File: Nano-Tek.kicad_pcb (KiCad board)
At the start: 4 copper layers, 55 x 42 mm, 47 parts, among them CN1 POWER_IN, CN2 USB, CN3 Floppy 34, J1 Sound, J2 USB_Prog, J3 OLED+SER, J4 Encoder, Q1 MMBT3904, U1 STM32F105RBT6, U2 74LCX07, U3 AP2112K-3.3, X1 8MHz

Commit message: Rev 1.1
OLED and Serial pin header changes.
Additional GND point for connecting 2 pin +5V input instead of using a Berg.
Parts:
- added J5: GND, Nano-Tek:GND_Pin, F.Cu at (88.5, 19.9)
- J3: value OLED+SER -> OLED; footprint Connector_PinHeader_2.54mm:PinHeader_1x06_P2.54mm_Vertical -> Connector_PinSocket_2.54mm:PinSocket_1x04_P2.54mm_Vertical
- J4: value Encoder -> Encoder+SER; footprint Connector_PinHeader_2.54mm:PinHeader_1x05_P2.54mm_Vertical -> Connector_PinHeader_2.54mm:PinHeader_1x07_P2.54mm_Vertical
- moved J4 10.8 mm to (41.6, 20.0)
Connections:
- J3 pad 1: SWCLK -> GND
- J3 pad 2: SWDIO -> +3V3
- J3 pad 3: GND -> SCL
- J3 pad 4: +3V3 -> SDA
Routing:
- net ENC_CLK: track 36.9 -> 45.0 mm
- net SDA: track 24.9 -> 19.1 mm
- net ENC_DT: track 35.5 -> 41.3 mm
- net SCL: track 19.9 -> 24.6 mm
- net ENC_SW: track 18.1 -> 22.1 mm
- net GND: vias 82 -> 83
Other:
- board text added: "+5V"
- board text added: "ENC"
- board text added: "Rev 1.1, August 2026 Schematics derived from OpenFlops design by SukkoPera Thanks to: Vinny, Mesarim, Screemo, Kavanoz, Wrangler, Ordyne"
- board text removed: "Rev 1.0, July 2026 Schematics derived from OpenFlops design by SukkoPera Thanks to: Vinny, Mesarim, Screemo, Kavanoz, Wrangler, Ordyne"

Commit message: Rev 1.1
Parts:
- moved J3 0.05 mm to (66.8, 20.0)
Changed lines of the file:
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@@
 	(footprint "Connector_PinSocket_2.54mm:PinSocket_1x04_P2.54mm_Vertical"
 		(layer "F.Cu")
-		(at 66.8 20.05 90)
+		(at 66.8 20 90)
 		(descr "Through hole straight socket strip, 1x04, 2.54mm pitch, single row (from Kicad 4.0.7), script generated")
 		(tags "Through hole socket strip THT 1x04 2.54mm single row")
 		(property "Reference" "J3"
-			(at 0 -2.77 90)
+			(at 0 -2.95 180)
 			(layer "F.SilkS")
 			(effects
@@
 		(tags "Through hole pin header THT 1x07 2.54mm single row")
 		(property "Reference" "J4"
-			(at 0 -2.38 90)
+			(at 0 17.92 180)
 			(layer "F.SilkS")
 			(effects
@@
 	)
 	(segment
-		(start 64.55 35.1)
-		(end 61.45 32)
-		(width 0.3)
-		(layer "F.Cu")
-		(net "SWCLK")
-	)
-	(segment
-		(start 62.75 43.175)
-		(end 62.75 42.275)
-		(width 0.3)
-		(layer "F.Cu")
-		(net "SWCLK")
-	)
-	(segment
-		(start 64.55 40.475)
-		(end 64.55 35.1)
-		(width 0.3)
-		(layer "F.Cu")
-		(net "SWCLK")
-	)
-	(segment
-		(start 61.45 24.58)
-		(end 56.87 20)
-		(width 0.3)
-		(layer "F.Cu")
-		(net "SWCLK")
-	)
-	(segment
-		(start 61.45 32)
-		(end 61.45 24.58)
-		(width 0.3)
-		(layer "F.Cu")
-		(net "SWCLK")
-	)
-	(segment
-		(start 62.75 42.275)
-		(end 64.55 40.475)
-		(width 0.3)
-		(layer "F.Cu")
-		(net "SWCLK")
-	)
-	(segment
-		(start 60.8 30.8)
-		(end 60.8 26.47)
-		(width 0.3)
-		(layer "F.Cu")
-		(net "SWDIO")
-	)
-	(segment
-		(start 62.5 40.25)
-		(end 60.825 40.25)
-		(width 0.3)
-		(layer "F.Cu")
-		(net "SWDIO")
-	)
-	(segment
-		(start 63.2 35.712939)
-		(end 63.2 39.55)
-		(width 0.3)
-		(layer "F.Cu")
-		(net "SWDIO")
-	)
-	(segment
-		(start 63.2 39.55)
-		(end 62.5 40.25)
-		(width 0.3)
-		(layer "F.Cu")
-		(net "SWDIO")
-	)
-	(segment
-		(start 62.034862 34.547801)
-		(end 63.2 35.712939)
-		(width 0.3)
-		(layer "F.Cu")
-		(net "SWDIO")
-	)
-	(segment
-		(start 60.8 26.47)
-		(end 54.33 20)
-		(width 0.3)
-		(layer "F.Cu")
-		(net "SWDIO")
-	)
-	(via
-		(at 62.034862 34.547801)
-		(size 0.6)
-		(drill 0.3)
-		(layers "F.Cu" "B.Cu")
-		(net "SWDIO")
-	)
-	(via
-		(at 60.8 30.8)
-		(size 0.6)
-		(drill 0.3)
-		(layers "F.Cu" "B.Cu")
-		(net "SWDIO")
-	)
-	(segment
-		(start 60.8 30.8)
-		(end 61.95 31.95)
-		(width 0.3)
-		(layer "B.Cu")
-		(net "SWDIO")
-	)
-	(segment
-		(start 61.95 34.462939)
-		(end 62.034862 34.547801)
-		(width 0.3)
-		(layer "B.Cu")
-		(net "SWDIO")
-	)
-	(segment
-		(start 61.95 31.95)
-		(end 61.95 34.462939)
-		(width 0.3)
-		(layer "B.Cu")
-		(net "SWDIO")
-	)
-	(segment
 		(start 64.25 31.825)
 		(end 64.25 27.85)
@@
 	)
 	(segment
-		(start 66.125 25.975)
-		(end 71.035 25.975)
+		(start 64.25 27.85)
+		(end 66.125 25.975)
 		(width 0.3)
 		(layer "F.Cu")
@@
 	)
 	(segment
-		(start 73.18 18.75)
-		(end 71.88 20.05)
+		(start 75.7 19.4)
+		(end 75.05 18.75)
 		(width 0.3)
 		(layer "F.Cu")
@@
 	)
 	(segment
-		(start 64.25 27.85)
-		(end 66.125 25.975)
+		(start 73.13 18.75)
+		(end 71.88 20)
 		(width 0.3)
 		(layer "F.Cu")
@@
 	)
 	(segment
-		(start 75.7 21.31)
-		(end 75.7 19.55)
+		(start 66.125 25.975)
+		(end 71.035 25.975)
 		(width 0.3)
 		(layer "F.Cu")
@@
 	)
 	(segment
-		(start 74.9 18.75)
-		(end 73.18 18.75)
+		(start 71.035 25.975)
+		(end 75.7 21.31)
 		(width 0.3)
 		(layer "F.Cu")
@@
 	)
 	(segment
-		(start 75.7 19.55)
-		(end 74.9 18.75)
+		(start 75.05 18.75)
+		(end 73.13 18.75)
 		(width 0.3)
 		(layer "F.Cu")
@@
 	)
 	(segment
-		(start 71.035 25.975)
-		(end 75.7 21.31)
+		(start 75.7 21.31)
+		(end 75.7 19.4)
 		(width 0.3)
 		(layer "F.Cu")
@@
 	)
 	(segment
-		(start 70.725 25.375)
-		(end 74.42 21.68)
+		(start 74.42 21.68)
+		(end 74.42 20)
 		(width 0.3)
 		(layer "F.Cu")
@@
 	)
 	(segment
-		(start 65.775 25.375)
-		(end 70.725 25.375)
+		(start 63.75 27.4)
+		(end 65.775 25.375)
 		(width 0.3)
 		(layer "F.Cu")
@@
 	)
 	(segment
-		(start 63.75 31.825)
-		(end 63.75 27.4)
+		(start 70.725 25.375)
+		(end 74.42 21.68)
 		(width 0.3)
 		(layer "F.Cu")
@@
 	)
 	(segment
-		(start 74.42 21.68)
-		(end 74.42 20.05)
+		(start 63.75 31.825)
+		(end 63.75 27.4)
 		(width 0.3)
 		(layer "F.Cu")
@@
 	)
 	(segment
-		(start 63.75 27.4)
-		(end 65.775 25.375)
+		(start 65.775 25.375)
+		(end 70.725 25.375)
 		(width 0.3)
 		(layer "F.Cu")
@@
 	)
 	(segment
+		(start 60.8 30.8)
+		(end 60.8 26.47)
+		(width 0.3)
+		(layer "F.Cu")
+		(net "SWDIO")
+	)
+	(segment
+		(start 62.5 40.25)
+		(end 60.825 40.25)
+		(width 0.3)
+		(layer "F.Cu")
+		(net "SWDIO")
+	)
+	(segment
+		(start 63.2 35.712939)
+		(end 63.2 39.55)
+		(width 0.3)
+		(layer "F.Cu")
+		(net "SWDIO")
+	)
+	(segment
+		(start 63.2 39.55)
+		(end 62.5 40.25)
+		(width 0.3)
+		(layer "F.Cu")
+		(net "SWDIO")
+	)
+	(segment
+		(start 62.034862 34.547801)
+		(end 63.2 35.712939)
+		(width 0.3)
+		(layer "F.Cu")
+		(net "SWDIO")
+	)
+	(segment
+		(start 60.8 26.47)
+		(end 54.33 20)
+		(width 0.3)
+		(layer "F.Cu")
+		(net "SWDIO")
+	)
+	(via
+		(at 62.034862 34.547801)
+		(size 0.6)
+		(drill 0.3)
+		(layers "F.Cu" "B.Cu")
+		(net "SWDIO")
+	)
+	(via
+		(at 60.8 30.8)
+		(size 0.6)
+		(drill 0.3)
+		(layers "F.Cu" "B.Cu")
+		(net "SWDIO")
+	)
+	(segment
+		(start 60.8 30.8)
+		(end 61.95 31.95)
+		(width 0.3)
+		(layer "B.Cu")
+		(net "SWDIO")
+	)
+	(segment
+		(start 61.95 34.462939)
+		(end 62.034862 34.547801)
+		(width 0.3)
+		(layer "B.Cu")
+		(net "SWDIO")
+	)
+	(segment
+		(start 61.95 31.95)
+		(end 61.95 34.462939)
+		(width 0.3)
+		(layer "B.Cu")
+		(net "SWDIO")
+	)
+	(segment
+		(start 64.55 35.1)
+		(end 61.45 32)
+		(width 0.3)
+		(layer "F.Cu")
+		(net "SWCLK")
+	)
+	(segment
+		(start 62.75 43.175)
+		(end 62.75 42.275)
+		(width 0.3)
+		(layer "F.Cu")
+		(net "SWCLK")
+	)
+	(segment
+		(start 64.55 40.475)
+		(end 64.55 35.1)
+		(width 0.3)
+		(layer "F.Cu")
+		(net "SWCLK")
+	)
+	(segment
+		(start 61.45 24.58)
+		(end 56.87 20)
+		(width 0.3)
+		(layer "F.Cu")
+		(net "SWCLK")
+	)
+	(segment
+		(start 61.45 32)
+		(end 61.45 24.58)
+		(width 0.3)
+		(layer "F.Cu")
+		(net "SWCLK")
+	)
+	(segment
+		(start 62.75 42.275)
+		(end 64.55 40.475)
+		(width 0.3)
+		(layer "F.Cu")
+		(net "SWCLK")
+	)
+	(segment

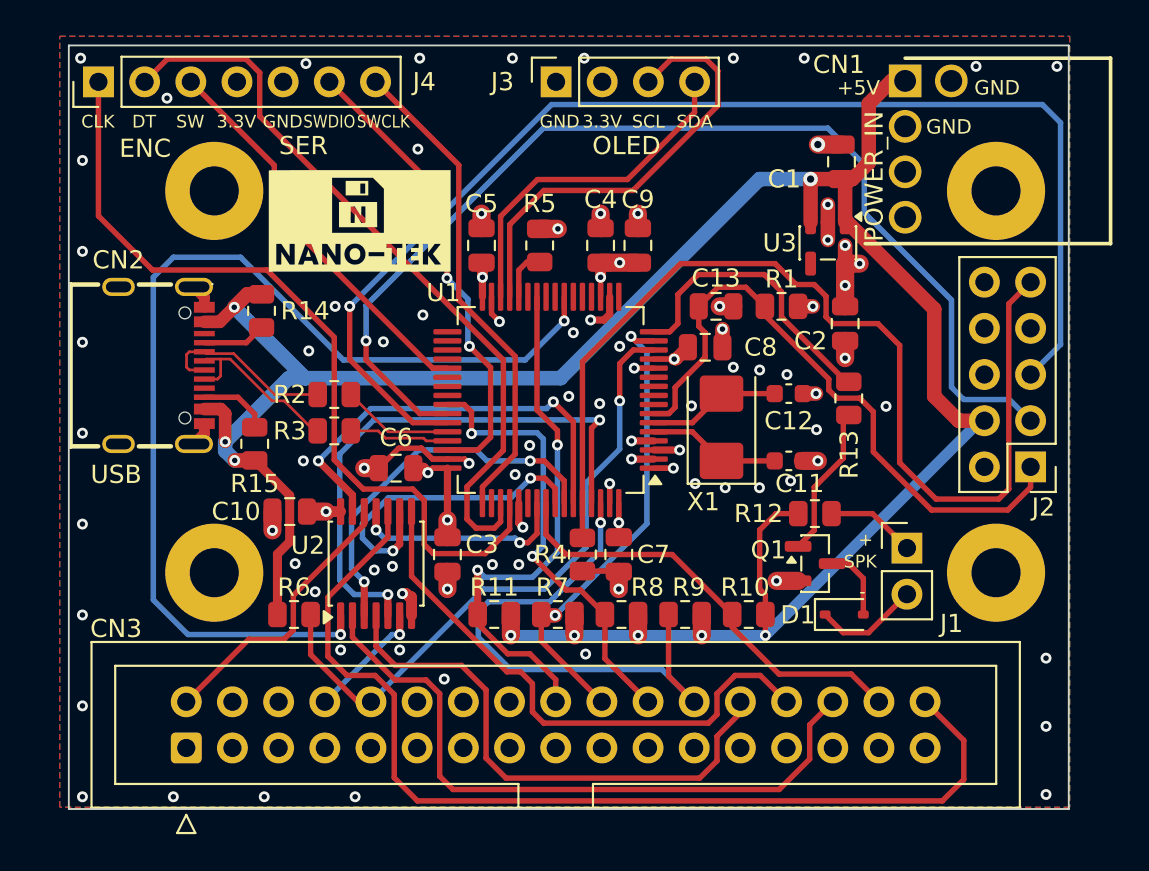
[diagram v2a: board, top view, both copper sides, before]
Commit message: Rev 1.2
Board shrunk to the length of the floppy header.
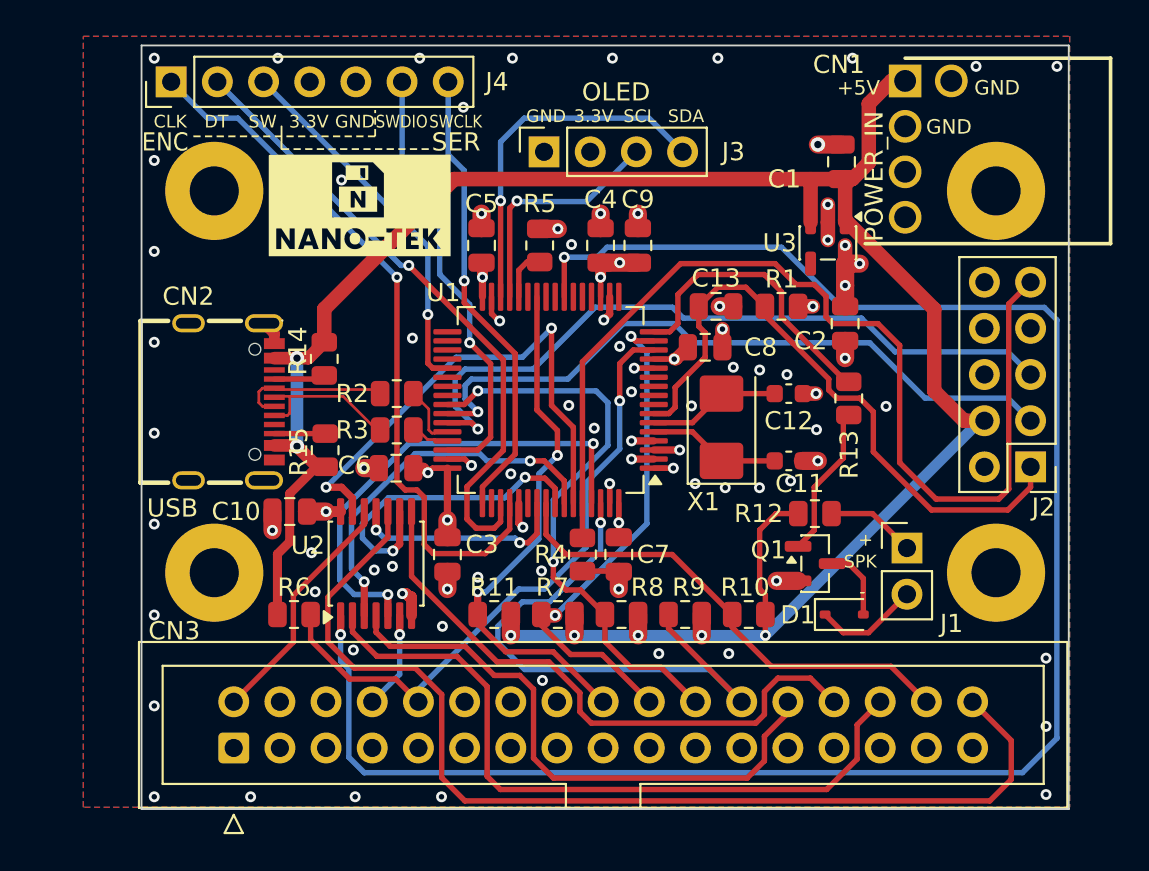
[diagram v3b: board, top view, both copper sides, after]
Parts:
- moved R14 4.34 mm to (54.0, 35.2)
- moved CN2 4.34 mm to (48.9, 37.6)
- moved J4 4.00 mm to (45.6, 20.0)
- moved J3 3.91 mm to (66.1, 23.9)
- moved R15 3.89 mm to (54.1, 40.3)
- moved R2 3.44 mm to (58.0, 37.1)
- moved R3 3.44 mm to (58.0, 39.1)
- moved LOGO2 2.62 mm to (69.7, 37.6)
- moved CN3 2.61 mm to (49.1, 56.6)
- moved LOGO1 0.85 mm to (56.0, 26.8)
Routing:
- net _DKRD_3V: track 57.5 -> 102.2 mm
- net TXD: track 68.4 -> 39.9 mm
- net RXD: track 60.3 -> 38.2 mm
- net SCL: track 24.7 -> 13.2 mm, vias 0 -> 1
- net +5V: track 135.3 -> 125.3 mm, vias 9 -> 7
- net _DKWD: track 24.6 -> 31.8 mm
- net ENC_DT: track 41.3 -> 34.9 mm, vias 0 -> 1
- net GND: track 39.0 -> 32.7 mm, vias 83 -> 80
- net ENC_CLK: track 45.0 -> 39.5 mm, vias 0 -> 1
- net _CHNG_3V: track 23.9 -> 28.6 mm
- net _INDEX_3V: track 30.9 -> 26.7 mm
- net USB_ST_D+: track 5.54 -> 2.13 mm
- net USB_ST_D-: track 6.16 -> 3.48 mm
- net _DKRD: track 36.8 -> 39.5 mm
- net _SIDE: track 24.3 -> 26.9 mm
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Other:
- board size 55 x 42 mm -> 51 x 42 mm
- board text added: "Rev 1.2, August 2026 Schematics derived from OpenFlops design by SukkoPera Thanks to: Vinny, Mesarim, Screemo, Kavanoz, Wrangler, Ordyne"
- board text removed: "Rev 1.1, August 2026 Schematics derived from OpenFlops design by SukkoPera Thanks to: Vinny, Mesarim, Screemo, Kavanoz, Wrangler, Ordyne"

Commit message: Rev 1.3
Various updates listed in readme file
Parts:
- removed LOGO1: LOGO, Nano-Tek:NanoTek_Logo_Stacked_10mm
- added C14: 10uF, Capacitor_SMD:C_0805_2012Metric, F.Cu at (58.1, 35.1)
- added C15: 10uF, Capacitor_SMD:C_0805_2012Metric, F.Cu at (51.9, 44.1)
- added C16: 47uF 10V, Capacitor_SMD:C_1206_3216Metric, F.Cu at (54.1, 44.6)
- added D2: B5819W SL, Diode_SMD:D_SOD-123, F.Cu at (54.7, 35.0)
- added R16: 10K, Resistor_SMD:R_0805_2012Metric, F.Cu at (74.2, 20.2)
- added R17: 10K, Resistor_SMD:R_0805_2012Metric, F.Cu at (56.5, 45.8)
- added R18: 10K, Resistor_SMD:R_0805_2012Metric, F.Cu at (82.7, 37.4)
- added R19: 10K, Resistor_SMD:R_0805_2012Metric, F.Cu at (82.7, 41.0)
- added R20: 10K, Resistor_SMD:R_0805_2012Metric, F.Cu at (78.4, 20.2)
- added R21: 1K, Resistor_SMD:R_0805_2012Metric, F.Cu at (63.9, 46.9)
- added U4: SY6288DAAC, Package_TO_SOT_SMD:SOT-23-5, F.Cu at (49.1, 30.9)
- J1: value Sound -> Buzzer; footprint Connector_PinHeader_2.54mm:PinHeader_1x02_P2.54mm_Vertical -> Nano-Tek:BUZ-TH_BD9.0-P4.00-D0.6-FD
- J4: footprint Connector_PinHeader_2.54mm:PinHeader_1x07_P2.54mm_Vertical -> Connector_PinHeader_2.54mm:PinHeader_1x08_P2.54mm_Vertical
- moved J1 34.6 mm to (56.2, 28.3), turned to 180 degrees
- moved C10 28.5 mm to (80.7, 43.7)
- moved U2 28.3 mm to (85.2, 46.5)
- moved R6 25.2 mm to (77.4, 46.2), turned to 0 degrees
- moved D1 23.5 mm to (76.1, 26.8)
- moved R12 17.6 mm to (78.9, 26.2), turned to 90 degrees
- moved Q1 17.5 mm to (76.9, 29.6)
- moved R13 12.3 mm to (73.4, 29.6), turned to 90 degrees
- moved R14 9.22 mm to (46.0, 30.8)
- moved C6 0.95 mm to (58.0, 42.2)
- moved R2 0.95 mm to (58.0, 38.1)
- moved R3 0.95 mm to (58.0, 40.1)
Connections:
- CN2 pad A4B9: +5V -> VBUS
- CN2 pad B4A9: +5V -> VBUS
- CN3 pad 16: unconnected-(CN3-Pin_16-Pad16) -> /MOTOR
- D1 pad 1: SPK- -> SPK+
- D1 pad 2: Net-(D1-A) -> SPK-
- Q1 pad 3: Net-(D1-A) -> SPK-
- R14 pad 2: +5V -> VBUS
- R15 pad 2: +5V -> VBUS
- U1 pad 17: unconnected-(U1-PA3-Pad17) -> Net-(U1-PA3)
- U1 pad 20: unconnected-(U1-PA4-Pad20) -> _USB_PWR_EN
- U1 pad 21: unconnected-(U1-PA5-Pad21) -> _USB_PWR_FLT
- U1 pad 42: RXD -> TXD
- U1 pad 43: TXD -> RXD
- U1 pad 50: unconnected-(U1-PA15-Pad50) -> /MOTOR
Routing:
- net NRST: track 35.0 -> 85.0 mm
- net _DKRD_3V: track 102.2 -> 53.7 mm
- net _CHNG: track 13.4 -> 58.5 mm, vias 0 -> 1
- net _USB_PWR_EN: track 0.00 -> 41.4 mm, vias 0 -> 4
- net _USB_PWR_FLT: track 0.00 -> 39.9 mm, vias 0 -> 3
- net VBUS: track 0.00 -> 38.1 mm
- net _RDY: track 58.1 -> 22.4 mm
- net _INDEX: track 5.36 -> 40.8 mm
- net _DKRD: track 39.5 -> 5.01 mm
- net SPK-: track 5.79 -> 32.8 mm, vias 0 -> 2
- net _TRK0: track 32.0 -> 12.3 mm
- net SPK+: track 4.93 -> 22.7 mm
- net Net-(U1-PA3): track 0.00 -> 16.8 mm, vias 0 -> 2
- net _WPROT: track 33.1 -> 16.8 mm
- net BOOT0: track 57.3 -> 41.0 mm, vias 0 -> 1
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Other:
- board text added: "1"
- board text added: "RST"
- board text added: "Rev 1.3, October 2026 Schematics derived from OpenFlops design by SukkoPera Thanks to: Vinny, Mesarim, Screemo, Kavanoz, Wrangler, Ordyne"
- board text removed: "+"
- board text removed: "-"
- board text removed: "Rev 1.2, August 2026 Schematics derived from OpenFlops design by SukkoPera Thanks to: Vinny, Mesarim, Screemo, Kavanoz, Wrangler, Ordyne"
- board text removed: "SPK"

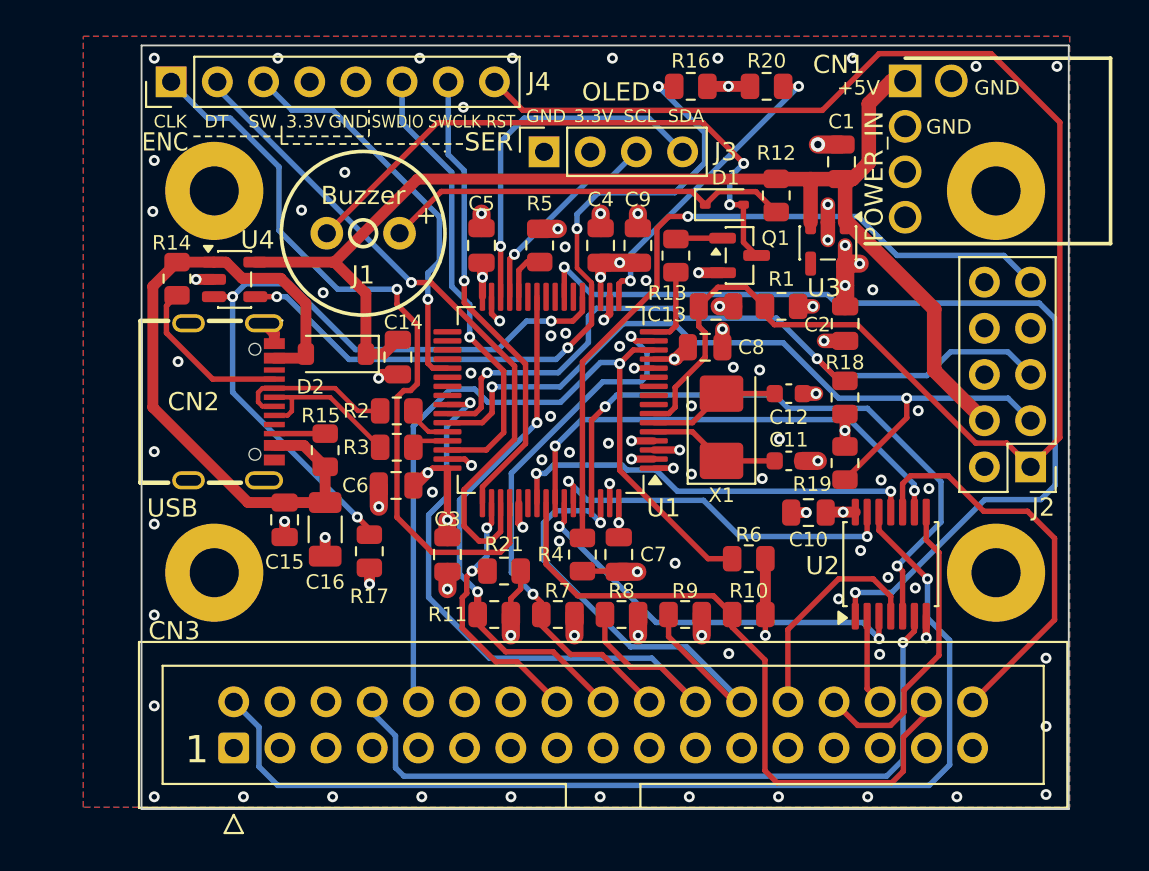
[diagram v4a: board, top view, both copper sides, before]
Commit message: Rev 1.3 with Rotated Floppy Header
Rev 1.3 with Rotated Floppy Header for better fit in some Amiga models
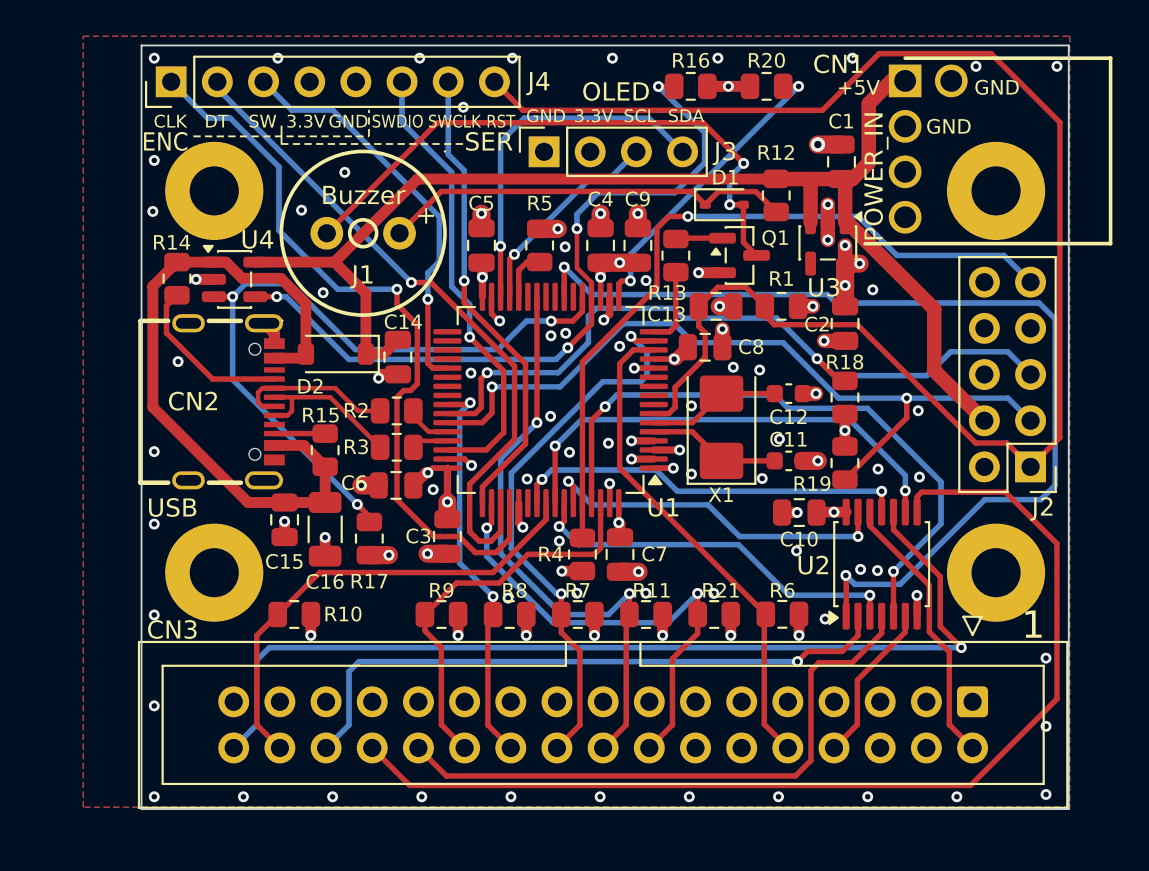
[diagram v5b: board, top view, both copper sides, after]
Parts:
- moved CN3 40.7 mm to (89.7, 54.1), turned to -90 degrees
- moved R10 25.0 mm to (52.4, 49.3)
- moved R9 13.4 mm to (60.5, 49.3)
- moved R21 11.8 mm to (75.5, 49.3)
- moved R11 8.35 mm to (71.8, 49.3)
- moved R8 6.15 mm to (64.2, 49.3)
- moved LOGO2 4.83 mm to (69.7, 32.8)
- moved R6 3.58 mm to (79.2, 49.3)
- moved R7 1.10 mm to (68.0, 49.3)
- moved C3 0.99 mm to (60.8, 45.0)
- moved R17 0.70 mm to (56.5, 45.1)
- moved C10 0.50 mm to (80.2, 43.7)
- moved U2 0.50 mm to (84.7, 46.5)
- moved C7 0.07 mm to (70.3, 46.0)
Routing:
- net _CHNG: track 58.5 -> 15.3 mm, vias 1 -> 0
- net _WPROT: track 16.8 -> 58.8 mm
- net _INDEX: track 40.8 -> 8.87 mm, vias 1 -> 0
- net _RDY: track 22.4 -> 53.4 mm, vias 0 -> 1
- net _DKRD: track 5.01 -> 34.6 mm, vias 0 -> 1
- net _TRK0: track 12.3 -> 33.2 mm
- net _SEL0: track 45.0 -> 27.2 mm, vias 1 -> 0
- net _DKWD: track 37.9 -> 21.9 mm, vias 1 -> 2
- net /MOTOR: track 15.3 -> 26.4 mm
- net _SIDE: track 36.6 -> 26.2 mm
- net +5V: track 112.3 -> 121.0 mm, vias 5 -> 7
- net _DKWE: track 28.0 -> 21.9 mm, vias 1 -> 0
- net DIR: track 28.9 -> 33.0 mm
- net _TRK0_3V: track 22.8 -> 21.2 mm
- net _DKRD_3V: track 53.7 -> 55.2 mm
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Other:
- board text added: "Rev 1.3 (Rotated Floppy Header), October 2026 Schematics derived from OpenFlops design by SukkoPera Thanks to: Vinny, Mesarim, Screemo, Kavanoz, Wrangler, Ordyne"
- board text removed: "Rev 1.3, October 2026 Schematics derived from OpenFlops design by SukkoPera Thanks to: Vinny, Mesarim, Screemo, Kavanoz, Wrangler, Ordyne"
